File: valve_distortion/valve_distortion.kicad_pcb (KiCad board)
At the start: 2 copper layers, 116.8 x 31.8 mm, 30 parts, among them J1 INPUT, J2 OUTPUT, J3 Barrel_Jack, SW1 SW_DPDT_x2, U1 12AX7, U2 TL074

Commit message: Finish layout
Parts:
- added C10: 0.1uF, Capacitor_THT:C_Disc_D3.0mm_W1.6mm_P2.50mm, F.Cu at (143.5, 82.6)
- added D3: 1N5817, Diode_THT:D_DO-41_SOD81_P10.16mm_Horizontal, F.Cu at (115.6, 85.1)
- added Q1: 2N3904, Package_TO_SOT_THT:TO-92_Inline, F.Cu at (156.2, 96.5)
- added R10: 100k, Resistor_THT:R_Axial_DIN0207_L6.3mm_D2.5mm_P10.16mm_Horizontal, F.Cu at (141.0, 82.6)
- added R11: 100k, Resistor_THT:R_Axial_DIN0207_L6.3mm_D2.5mm_P10.16mm_Horizontal, F.Cu at (141.0, 87.6)
- added R12: 470R, Resistor_THT:R_Axial_DIN0207_L6.3mm_D2.5mm_P10.16mm_Horizontal, F.Cu at (162.6, 96.5)
- added R13: 100k, Resistor_THT:R_Axial_DIN0207_L6.3mm_D2.5mm_P10.16mm_Horizontal, F.Cu at (130.8, 90.2)
- C5: value 1uF -> 16pF; footprint Capacitor_THT:CP_Radial_D4.0mm_P2.00mm -> Capacitor_THT:C_Disc_D3.0mm_W1.6mm_P2.50mm
- C8: value 10uF -> 1uF; footprint Capacitor_THT:CP_Radial_D5.0mm_P2.50mm -> Capacitor_THT:CP_Radial_D4.0mm_P2.00mm
- C9: value 0.1uF -> 10uF; footprint Capacitor_THT:C_Disc_D3.0mm_W1.6mm_P2.50mm -> Capacitor_THT:CP_Radial_D5.0mm_P2.50mm
- D1: value ENABLE -> LED IND 12V
- D2: value SIGNAL -> NTE30033
- J1, J2: footprint Connector_Molex:Molex_KK-254_AE-6410-02A_1x02_P2.54mm_Vertical -> Connector_PinHeader_2.54mm:PinHeader_1x02_P2.54mm_Vertical
- R2: value 220K -> 100R
- R3: value 100k -> 220K
- R6, R7: value 1k -> 100k
- RV4: value R_Potentiometer_Trim -> 200k; footprint Potentiometer_THT:Potentiometer_Bourns_3266Y_Vertical -> valve_distortion:Trimmer
- moved R1 75.4 mm to (172.7, 77.5), turned to 180 degrees
- moved R6 71.7 mm to (146.1, 87.6), turned to 0 degrees
- moved D1 46.4 mm to (120.7, 99.1), turned to 90 degrees
- moved J2 43.3 mm to (94.0, 99.1), turned to 90 degrees
- moved C1 28.5 mm to (123.2, 74.9)
- moved R5 28.0 mm to (162.6, 92.7), turned to 0 degrees
- moved R8 25.9 mm to (156.2, 82.6), turned to 180 degrees
- moved C9 22.5 mm to (120.7, 85.1), turned to 90 degrees
- moved C6 21.8 mm to (156.2, 74.4), turned to 90 degrees
- moved R2 20.6 mm to (172.7, 74.9), turned to 180 degrees
- moved D2 19.2 mm to (177.8, 99.1)
- moved J3 18.2 mm to (105.4, 97.8), turned to 0 degrees
- moved C5 13.3 mm to (153.7, 80.0), turned to 90 degrees
- moved R4 12.2 mm to (172.7, 90.2)
- moved R7 12.1 mm to (156.2, 85.1), turned to 180 degrees
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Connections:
- C5 pad 1: Net-(C5-Pad1) -> /BUF_OUT
- C5 pad 2: Net-(C5-Pad2) -> Net-(R6-Pad1)
- C6 pad 1: Net-(R8-Pad2) -> /BUF_OUT
- C6 pad 2: GND -> Net-(C6-Pad2)
- C7 pad 1: /VBIAS -> Net-(C7-Pad1)
- C8 pad 1: +12V -> Net-(C8-Pad1)
- D1 pad 1: GND -> /ENABLE
- D1 pad 2: Net-(D1-Pad2) -> GND
- D2 pad 1: GND -> Net-(D2-Pad1)
- D2 pad 2: Net-(R7-Pad2) -> Net-(D2-Pad2)
- J3 pad 1: +12V -> Net-(J3-Pad1)
- R2 pad 1: +12V -> Net-(R2-Pad1)
- R2 pad 2: Net-(C2-Pad2) -> Net-(R2-Pad2)
- R3 pad 2: Net-(C3-Pad1) -> Net-(C2-Pad2)
- R5 pad 1: Net-(C3-Pad2) -> +12V
- R5 pad 2: /VBIAS -> Net-(C3-Pad1)
- R6 pad 1: Net-(D1-Pad2) -> Net-(R6-Pad1)
- R6 pad 2: Net-(R6-Pad2) -> Net-(C3-Pad2)
- R7 pad 1: Net-(U2-Pad7) -> Net-(R6-Pad1)
- R7 pad 2: Net-(R7-Pad2) -> VBIAS
- R8 pad 1: +12V -> /BUF_OUT
- R8 pad 2: Net-(R8-Pad2) -> Net-(R6-Pad1)
- R9 pad 1: Net-(R8-Pad2) -> +12V
- R9 pad 2: GND -> Net-(C7-Pad1)
- RV1 pad 3: Net-(RV1-Pad3) -> Net-(R2-Pad2)
- RV3 pad 3: Net-(C5-Pad2) -> Net-(C6-Pad2)
- RV4 pad 2: Net-(RV4-Pad2) -> Net-(U2-Pad13)
- SW1 pad 4: Net-(R6-Pad2) -> +12V
- SW1 pad 5: +12V -> /ENABLE
- SW1 pad 6: unconnected-(SW1-Pad6) -> GND
- U1 pad 1: Net-(C2-Pad2) -> Net-(C3-Pad1)
- U1 pad 2: Net-(C1-Pad1) -> Net-(C2-Pad1)
- U1 pad 3: Net-(RV1-Pad3) -> GND
- U1 pad 6: Net-(C3-Pad1) -> Net-(C2-Pad2)
- U1 pad 7: Net-(C2-Pad1) -> Net-(C1-Pad1)
- U1 pad 8: GND -> Net-(R2-Pad1)
- U2 pad 1: /VBIAS -> Net-(C8-Pad1)
- U2 pad 10: Net-(C3-Pad2) -> VBIAS
- U2 pad 12: /VBIAS -> /BUF_OUT
- U2 pad 14: Net-(U2-Pad13) -> Net-(R12-Pad1)
- U2 pad 2: /VBIAS -> Net-(C8-Pad1)
- U2 pad 3: Net-(R8-Pad2) -> Net-(C7-Pad1)
- U2 pad 5: Net-(C3-Pad2) -> VBIAS
- U2 pad 6: Net-(RV4-Pad2) -> Net-(R6-Pad1)
- U2 pad 7: Net-(U2-Pad7) -> /BUF_OUT
- U2 pad 8: Net-(C5-Pad1) -> Net-(U2-Pad8)
- U2 pad 9: Net-(C5-Pad1) -> Net-(U2-Pad8)
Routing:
- net Net-(RV1-Pad3): track 131.9 -> 0.00 mm, vias 2 -> 0
- net Net-(R2-Pad2): track 0.00 -> 104.3 mm, vias 0 -> 1
- net +12V: track 85.6 -> 165.5 mm, vias 0 -> 2
- net /INPUT: track 0.00 -> 73.1 mm, vias 0 -> 2
- net /ENABLE: track 0.00 -> 69.8 mm
- net Net-(RV3-Pad2): track 89.3 -> 135.9 mm, vias 0 -> 3
- net Net-(R12-Pad1): track 0.00 -> 46.3 mm, vias 0 -> 1
- net Net-(C3-Pad2): track 22.7 -> 60.1 mm, vias 0 -> 1
- net Net-(R6-Pad1): track 0.00 -> 31.1 mm, vias 0 -> 1
- net Net-(Q1-Pad2): track 0.00 -> 28.6 mm
- net /BUF_OUT: track 0.00 -> 27.6 mm
- net Net-(J2-PadT): track 0.00 -> 26.1 mm
- net GND: track 0.00 -> 23.0 mm, vias 0 -> 200
- net Net-(C1-Pad1): track 82.9 -> 60.8 mm
- net /VBIAS: track 21.7 -> 0.00 mm
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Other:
- board size 116.8 x 31.8 mm -> 116.8 x 38.1 mm
- board text added: "ENABLE"
- board text added: "JLCJLCJLCJLC"
- board text added: "Max Proskauer v0.1 Sept 2022"
- board text added: "VALVE DISTORTION PEDAL"
- board text added: "github.com/mprosk/valve_dist_pedal"

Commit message: Include changes from scehmatic review
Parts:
- added R14: 100k, Resistor_THT:R_Axial_DIN0207_L6.3mm_D2.5mm_P10.16mm_Horizontal, F.Cu at (130.8, 90.2)
- R12: value 470R -> 100k
- R13: value 100k -> 470R
- moved R13 32.4 mm to (162.6, 96.5), turned to 0 degrees
- moved R12 29.2 mm to (146.1, 72.4), turned to 180 degrees
- moved R9 25.4 mm to (156.2, 85.1), turned to 180 degrees
- moved R8 14.4 mm to (146.1, 92.7), turned to 0 degrees
- moved R10 11.4 mm to (130.8, 87.6), turned to 0 degrees
- moved R7 10.5 mm to (146.1, 87.6), turned to 0 degrees
- moved RV4 3.81 mm to (138.4, 90.2)
- moved R11 2.55 mm to (141.0, 85.1)
- moved C5 2.54 mm to (153.7, 82.6)
- moved C8 2.54 mm to (132.1, 82.6)
- moved C7 2.54 mm to (132.1, 78.1)
- moved U2 2.54 mm to (135.9, 82.5)
- moved C10 2.53 mm to (143.5, 85.1)
- moved R6 2.53 mm to (146.1, 90.2)
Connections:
- C5 pad 2: Net-(R6-Pad1) -> Net-(C5-Pad2)
- C8 pad 1: Net-(C8-Pad1) -> VBIAS
- R10 pad 1: Net-(C7-Pad1) -> +12V
- R10 pad 2: GND -> Net-(C7-Pad1)
- R11 pad 1: VBIAS -> Net-(C7-Pad1)
- R11 pad 2: Net-(C8-Pad1) -> GND
- R12 pad 1: Net-(R12-Pad1) -> Net-(U2-Pad10)
- R12 pad 2: Net-(D2-Pad2) -> VBIAS
- R13 pad 1: Net-(Q1-Pad2) -> Net-(R13-Pad1)
- R13 pad 2: /ENABLE -> Net-(D2-Pad2)
- R6 pad 1: Net-(R6-Pad1) -> Net-(C5-Pad2)
- R6 pad 2: Net-(C3-Pad2) -> VBIAS
- R7 pad 1: Net-(R6-Pad1) -> Net-(C5-Pad2)
- R7 pad 2: VBIAS -> Net-(C3-Pad2)
- R8 pad 1: /BUF_OUT -> Net-(U2-Pad5)
- R8 pad 2: Net-(R6-Pad1) -> VBIAS
- R9 pad 1: +12V -> /BUF_OUT
- R9 pad 2: Net-(C7-Pad1) -> Net-(C5-Pad2)
- U2 pad 1: Net-(C8-Pad1) -> VBIAS
- U2 pad 10: VBIAS -> Net-(U2-Pad10)
- U2 pad 14: Net-(R12-Pad1) -> Net-(R13-Pad1)
- U2 pad 2: Net-(C8-Pad1) -> VBIAS
- U2 pad 5: VBIAS -> Net-(U2-Pad5)
- U2 pad 6: Net-(R6-Pad1) -> Net-(C5-Pad2)
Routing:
- net Net-(R12-Pad1): track 46.3 -> 0.00 mm, vias 1 -> 0
- net Net-(R13-Pad1): track 0.00 -> 45.7 mm, vias 0 -> 1
- net Net-(R6-Pad1): track 31.1 -> 0.00 mm, vias 1 -> 0
- net VBIAS: track 19.9 -> 41.6 mm
- net Net-(C5-Pad2): track 0.00 -> 14.8 mm
- net Net-(C8-Pad1): track 14.5 -> 0.00 mm
- net Net-(U2-Pad5): track 0.00 -> 11.2 mm
- net +12V: track 165.5 -> 156.2 mm
- net Net-(RV4-Pad2): track 19.4 -> 16.3 mm
- net GND: track 23.0 -> 20.2 mm, vias 200 -> 182
- net Net-(U2-Pad10): track 0.00 -> 2.54 mm
- net /BUF_OUT: track 27.6 -> 28.7 mm
- net Net-(C3-Pad2): track 60.1 -> 59.5 mm

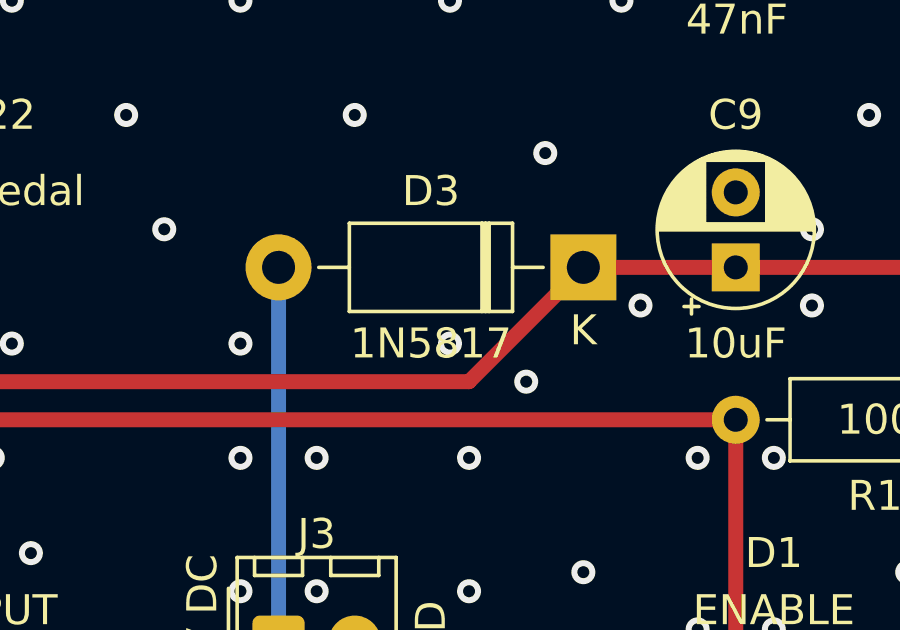
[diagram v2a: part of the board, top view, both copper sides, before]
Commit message: Address opamp cap load
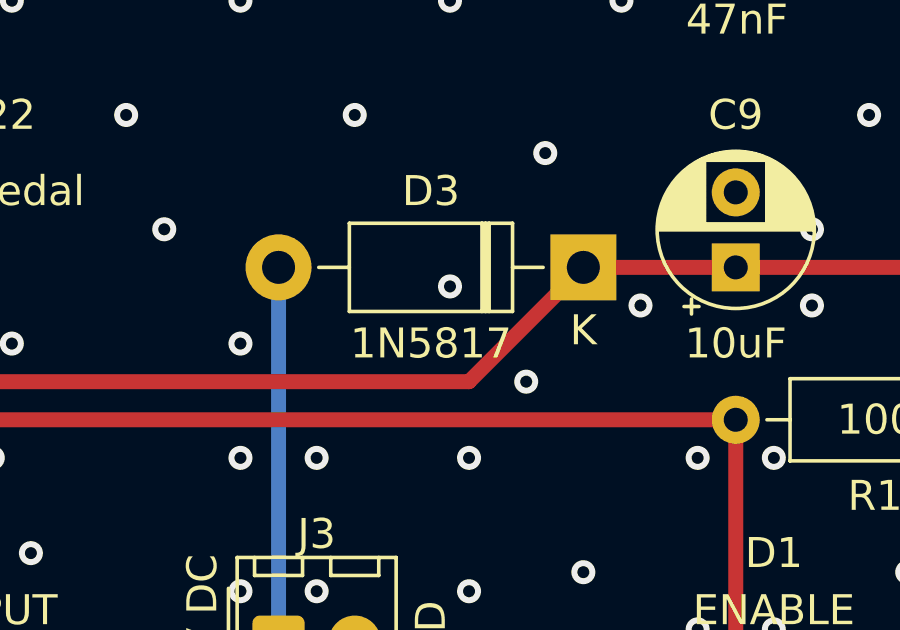
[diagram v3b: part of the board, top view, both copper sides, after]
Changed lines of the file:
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@@
   (via (at 119.38 70.485) (size 0.8) (drill 0.4) (layers "F.Cu" "B.Cu") (free) (net 7))
   (via (at 161.29 78.74) (size 0.8) (drill 0.4) (layers "F.Cu" "B.Cu") (free) (net 7))
-  (via (at 111.125 87.63) (size 0.8) (drill 0.4) (layers "F.Cu" "B.Cu") (free) (net 7))
+  (via (at 111.125 85.725) (size 0.8) (drill 0.4) (layers "F.Cu" "B.Cu") (free) (net 7))
   (via (at 64.77 67.945) (size 0.8) (drill 0.4) (layers "F.Cu" "B.Cu") (free) (net 7))
   (via (at 88.9 92.71) (size 0.8) (drill 0.4) (layers "F.Cu" "B.Cu") (free) (net 7))
